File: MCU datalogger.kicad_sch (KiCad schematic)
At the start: 25 parts, among them U1 24LC1025, U2 DS1337S+, U3 24LC1025, U4 ATMEGA328P-AU, Y1 32.768 KHz, Y2 16MHz

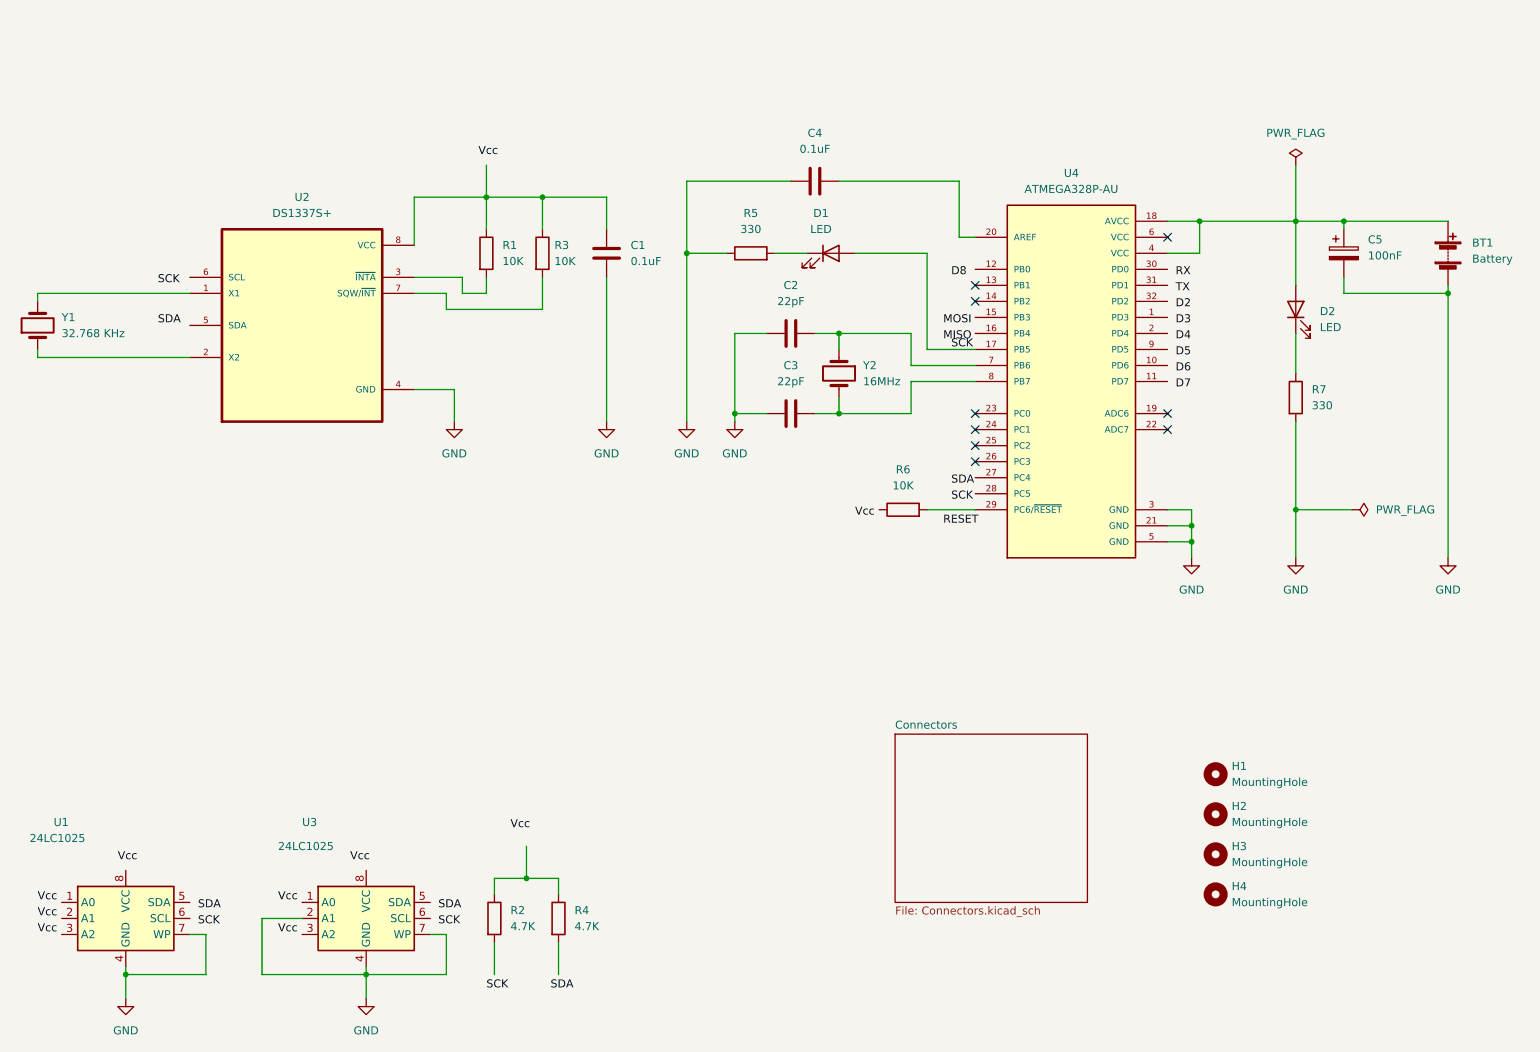
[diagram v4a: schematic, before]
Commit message: Completed wiring in tthe second sheet
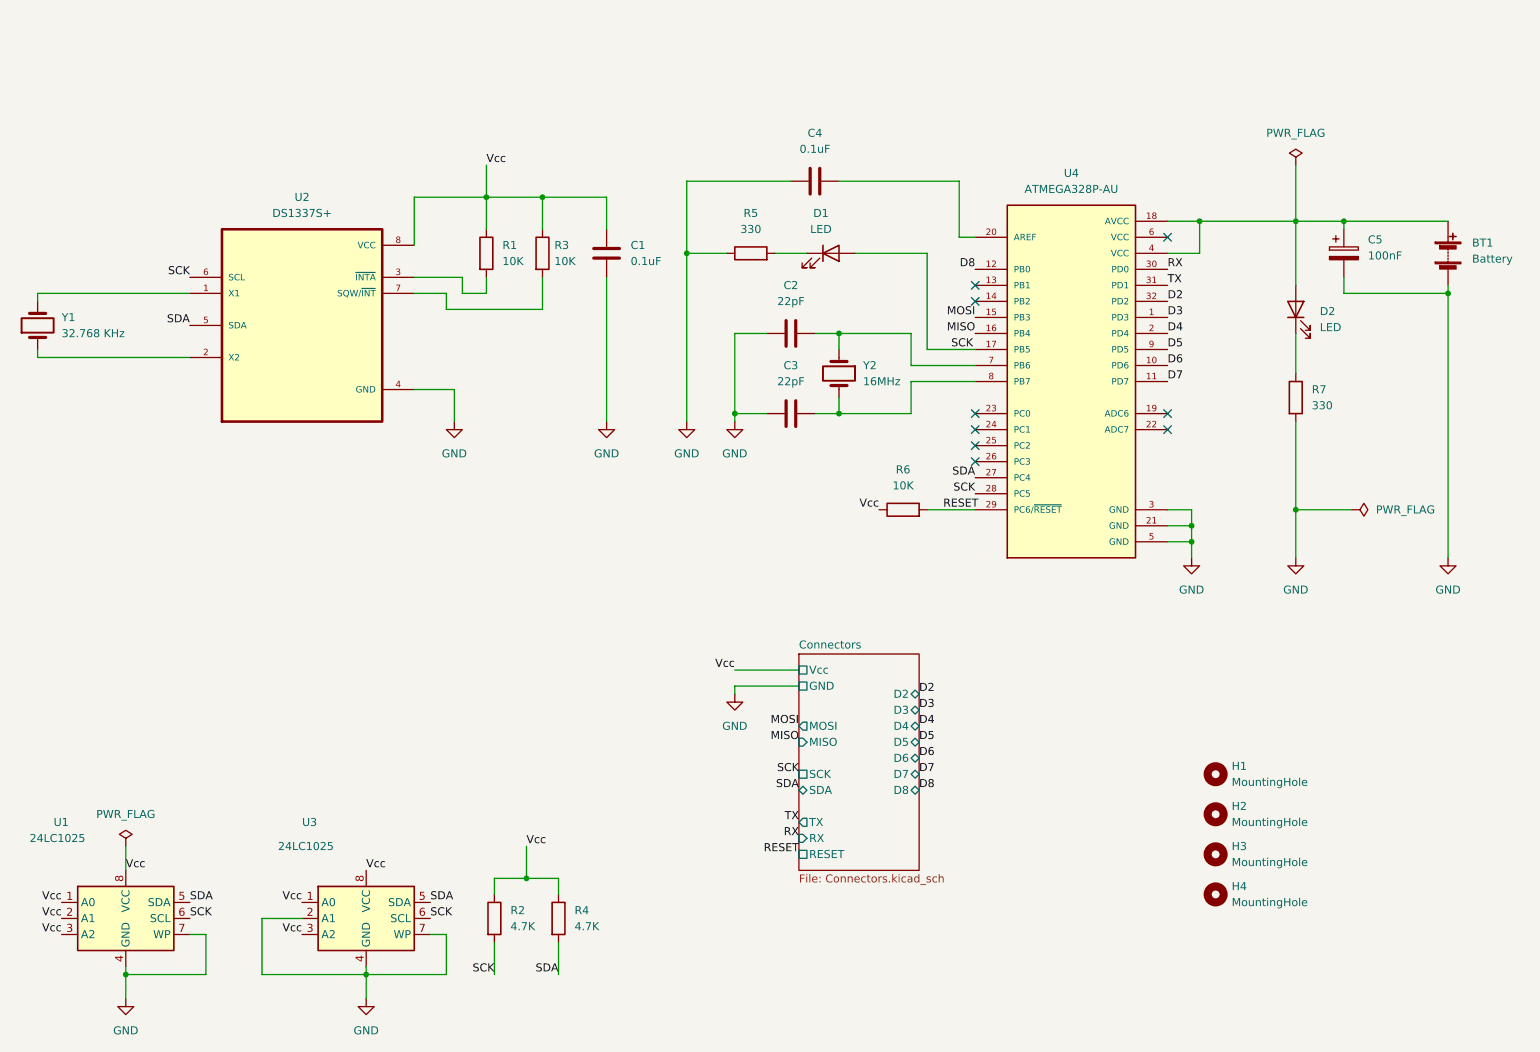
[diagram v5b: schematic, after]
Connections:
- net D2: now also U4.32 (PD2)
- net D3: now also U4.1 (PD3)
- net D4: now also U4.2 (PD4)
- net D5: now also U4.9 (PD5)
- net D6: now also U4.10 (PD6)
- net D7: now also U4.11 (PD7)
- net D8: now also U4.12 (PB0)
- net MISO: now also U4.16 (PB4)
- net MOSI: now also U4.15 (PB3)
- net RESET: now also R6.2, U4.29 (PC6/~{RESET})
- net RX: now also U4.30 (PD0)
- net SCK: now also R2.2, U1.6 (SCL), U2.6 (SCL), U3.6 (SCL), U4.28 (PC5)
- net SDA: now also R4.2, U1.5 (SDA), U2.5 (SDA), U3.5 (SDA), U4.27 (PC4)
- net TX: now also U4.31 (PD1)
- net Vcc: now also C1.1, R1.1, R2.1, R3.1, R4.1, R6.1, U1.1 (A0), U1.2 (A1), U1.3 (A2), U1.8 (VCC), U2.8 (VCC), U3.1 (A0), U3.3 (A2), U3.8 (VCC)
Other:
- sheet Connectors ports: added D2, D3, D4, D5, D6, D7, D8, GND, MISO, MOSI, RESET, RX, SCK, SDA, TX, Vcc; removed none
